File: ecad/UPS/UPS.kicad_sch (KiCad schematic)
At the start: 0 parts

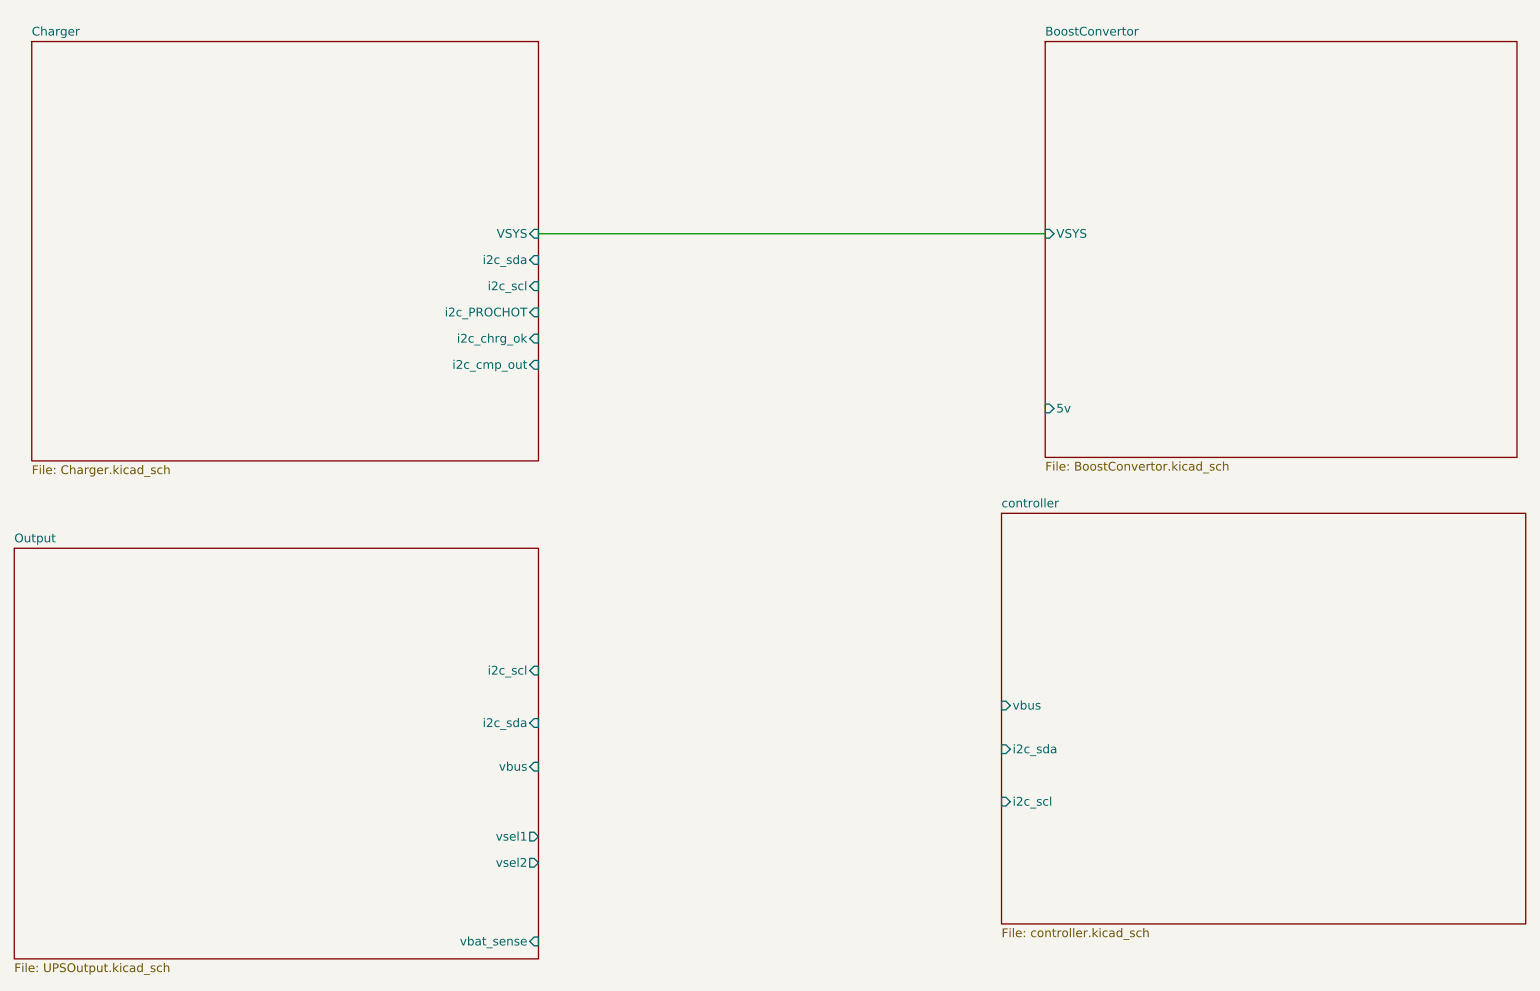
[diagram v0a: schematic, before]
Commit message: Add thermistors for batteries and link signals
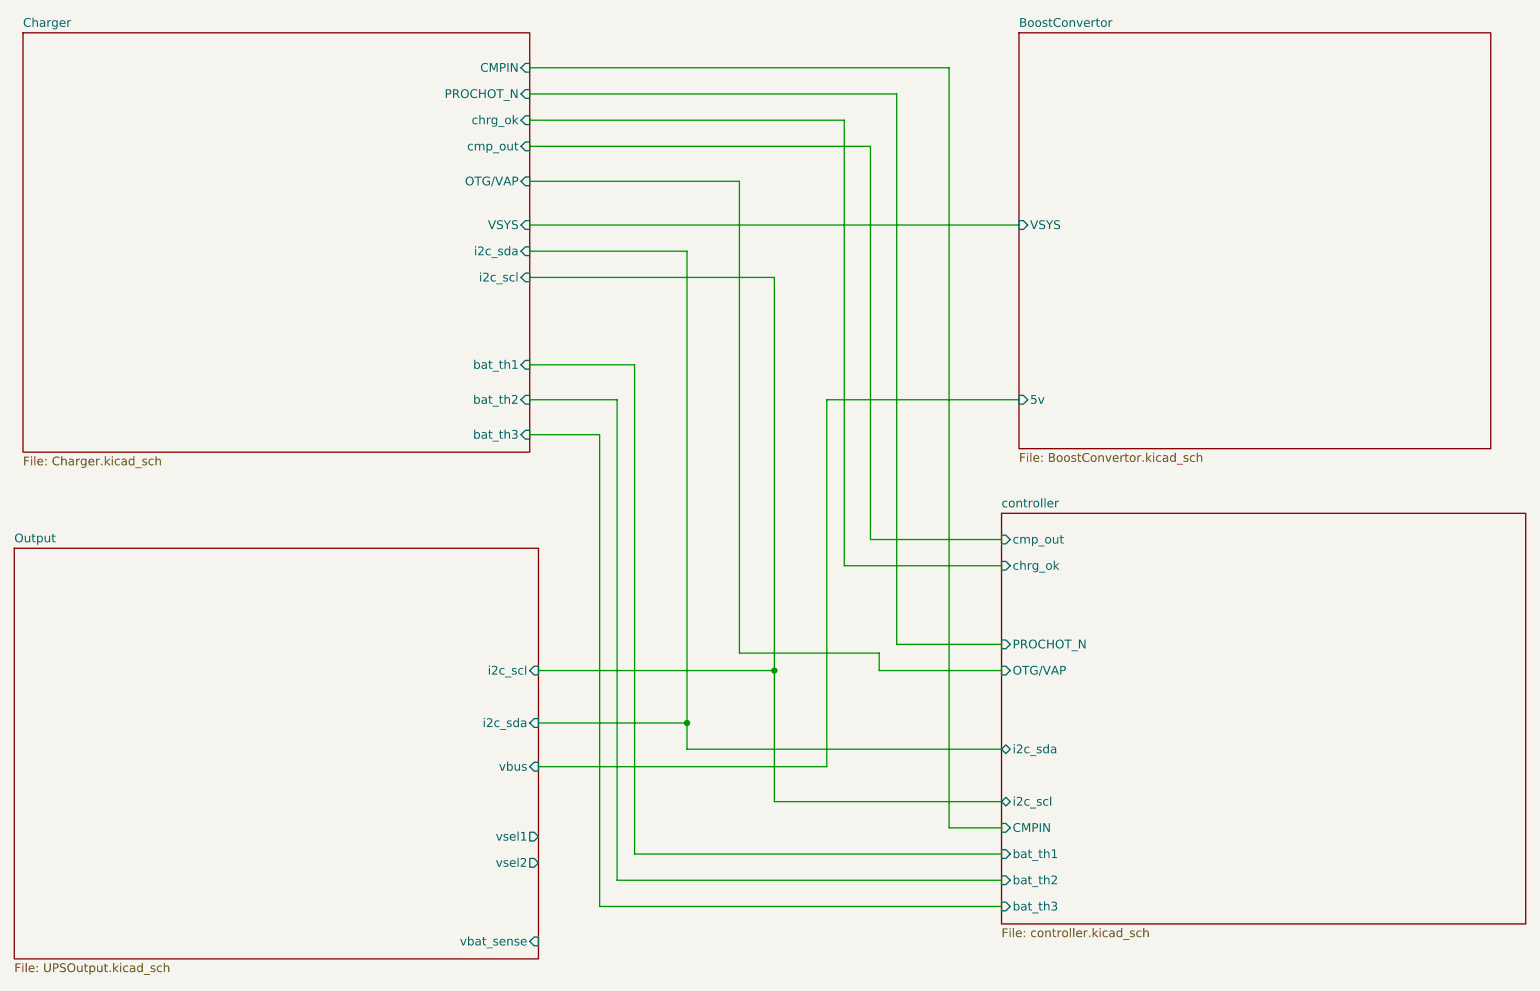
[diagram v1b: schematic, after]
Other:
- sheet Charger ports: added CMPIN, OTG/VAP, PROCHOT_N, bat_th1, bat_th2, bat_th3, chrg_ok, cmp_out; removed i2c_PROCHOT, i2c_chrg_ok, i2c_cmp_out
- sheet controller ports: added CMPIN, OTG/VAP, PROCHOT_N, bat_th1, bat_th2, bat_th3, chrg_ok, cmp_out; removed vbus
